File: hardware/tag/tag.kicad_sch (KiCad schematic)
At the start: 12 parts

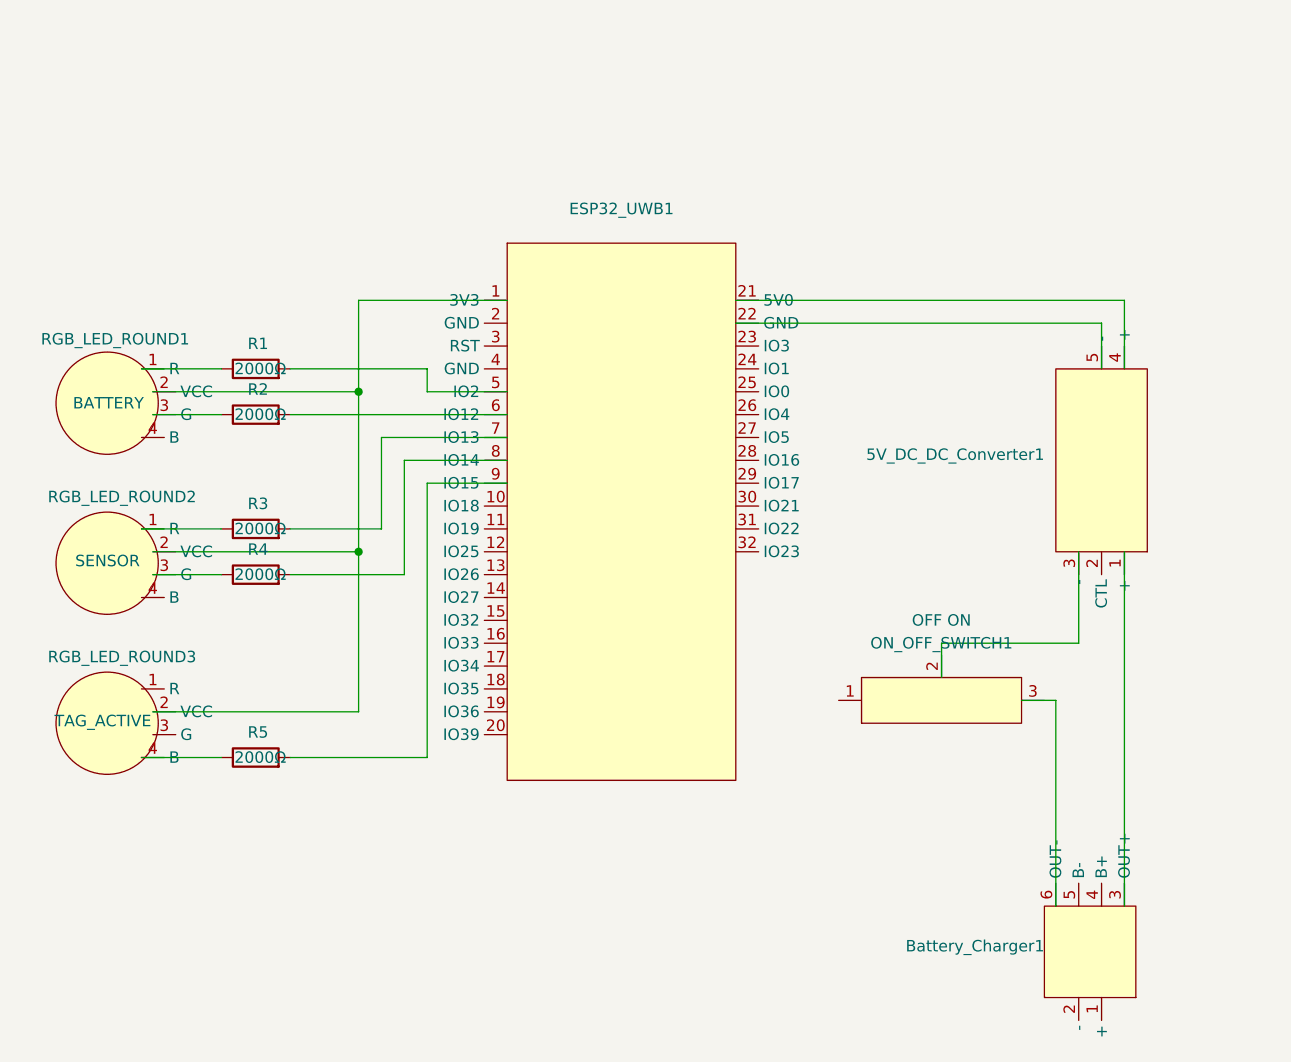
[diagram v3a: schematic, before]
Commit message: remote: Add battery status LED logic.
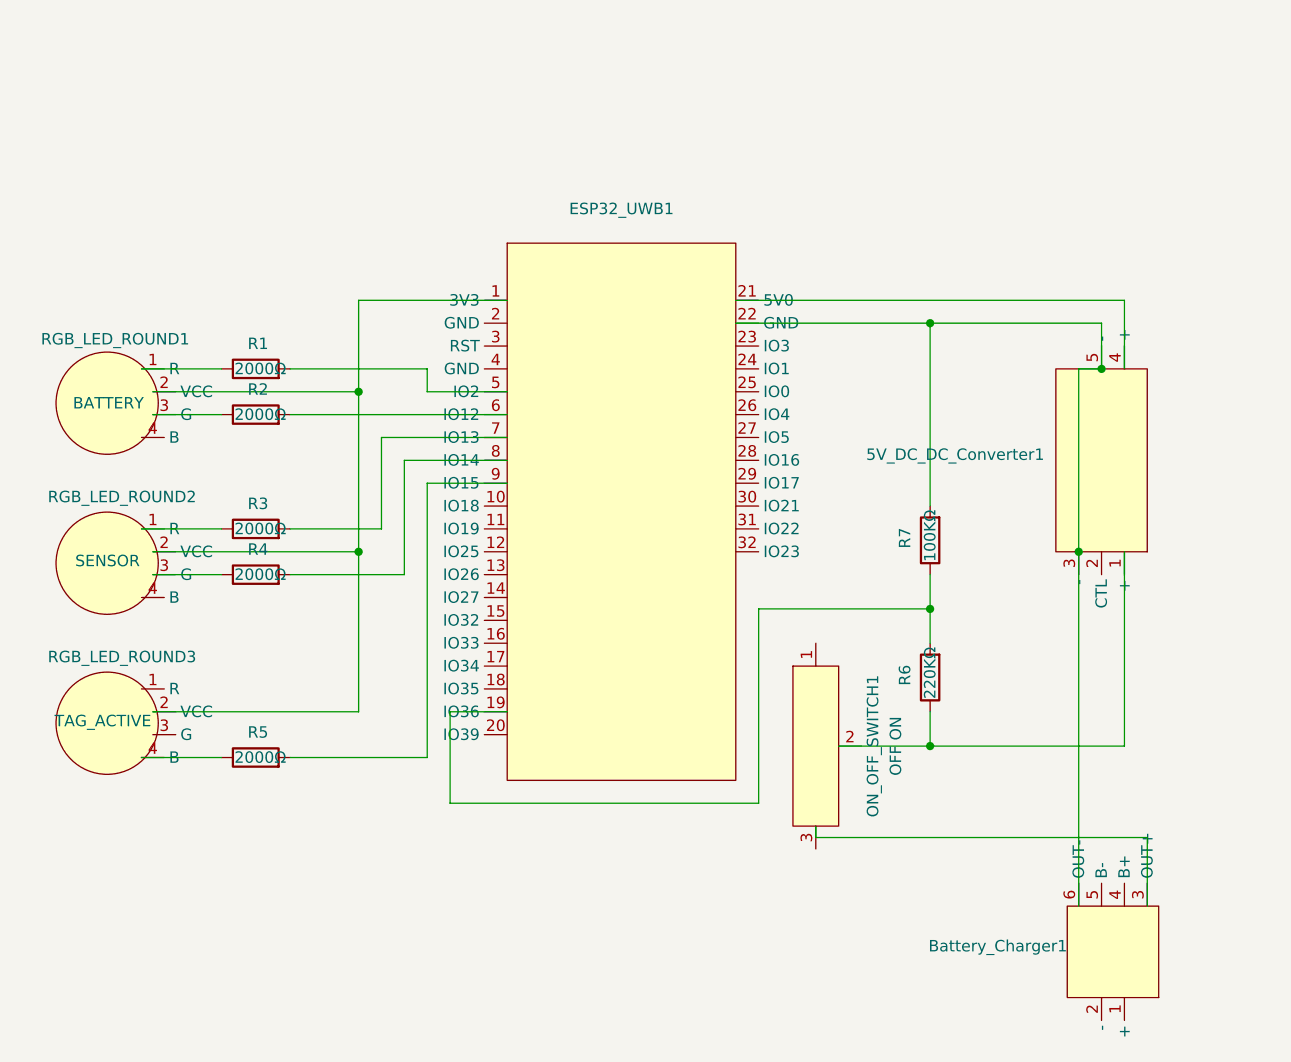
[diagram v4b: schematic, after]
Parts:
- added R6: 220KΩ, Autocam:Simple Resistor, symbol Autocam:Simple Resistor
- added R7: 100KΩ, Autocam:Simple Resistor, symbol Autocam:Simple Resistor
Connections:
- net at ESP32_UWB1.19 (IO36): now also R6.2, R7.1
- net at 5V_DC_DC_Converter1.5 (-), ESP32_UWB1.22 (GND): now also 5V_DC_DC_Converter1.3 (-), Battery_Charger1.6 (OUT-), R7.2
- net at 5V_DC_DC_Converter1.1 (+): now also ON_OFF_SWITCH1.2, R6.1; no longer Battery_Charger1.3 (OUT+)
- net at ON_OFF_SWITCH1.3: now also Battery_Charger1.3 (OUT+); no longer Battery_Charger1.6 (OUT-)
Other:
- moved on the sheet: Battery_Charger1, ON_OFF_SWITCH1

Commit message: hardware/tag: Remove the tag active led.
The tag has not turned on the BLE yet.
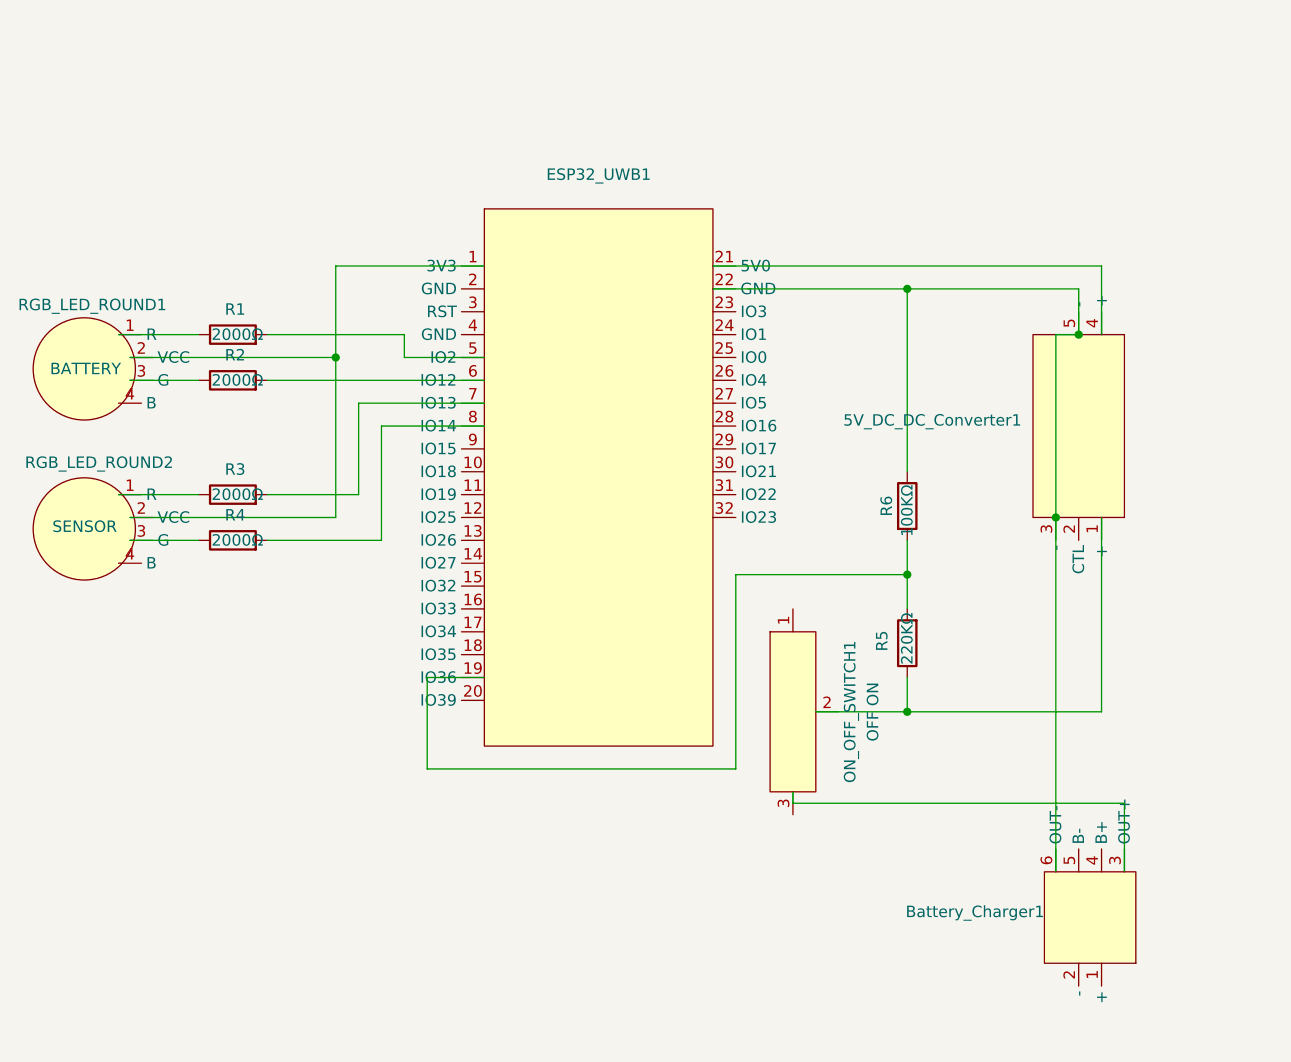
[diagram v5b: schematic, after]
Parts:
- removed R5: 2000Ω, Autocam:Simple Resistor, symbol Autocam:Simple Resistor
- removed RGB_LED_ROUND3: TAG_ACTIVE, Autocam:Anode RGB LED (Round), symbol Autocam:ANODE_RGB_LED_Round
- renumbered R6 to R5, R7 to R6
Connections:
- net at ESP32_UWB1.19 (IO36), R5.2: now also R6.2; no longer R6.1
- net at 5V_DC_DC_Converter1.3 (-), 5V_DC_DC_Converter1.5 (-), Battery_Charger1.6 (OUT-)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: now also R6.1; no longer R6.2
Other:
- moved on the sheet: 5V_DC_DC_Converter1, Battery_Charger1, ESP32_UWB1, ON_OFF_SWITCH1, R1, R2, R3, R4, R5, R6, RGB_LED_ROUND1, RGB_LED_ROUND2

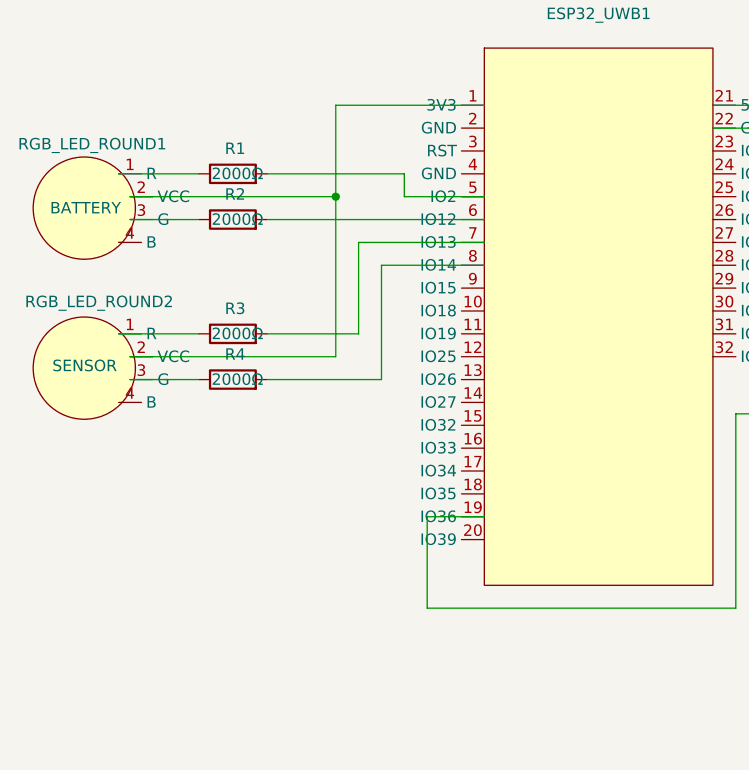
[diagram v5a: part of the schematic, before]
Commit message: hardware: Increase the LED resistor from 2000Ω to 10KΩ.
To reduce the power consumption.
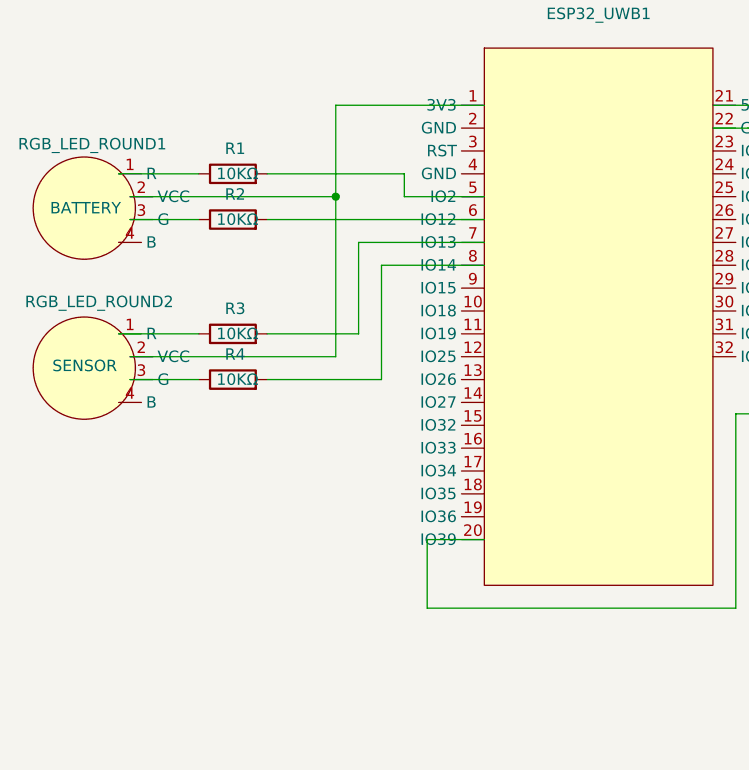
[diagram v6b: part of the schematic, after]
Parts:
- R1, R2, R3, R4: value 2000Ω -> 10KΩ
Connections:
- net at R5.2, R6.2: now also ESP32_UWB1.20 (IO39); no longer ESP32_UWB1.19 (IO36)
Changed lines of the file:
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@@
+	(wire
+		(pts
+			(xy 127 132.08) (xy 127 124.46)
+		)
+		(stroke
+			(width 0)
+			(type default)
+		)
+	)
 	(wire
 		(pts
@@
 	(wire
 		(pts
+			(xy 127 124.46) (xy 133.35 124.46)
+		)
+		(stroke
+			(width 0)
+			(type default)
+		)
+	)
+	(wire
+		(pts
 			(xy 116.84 76.2) (xy 133.35 76.2)
 		)
@@
 	(wire
 		(pts
-			(xy 133.35 121.92) (xy 127 121.92)
-		)
-		(stroke
-			(width 0)
-			(type default)
-		)
-	)
-	(wire
-		(pts
 			(xy 201.93 83.82) (xy 201.93 76.2)
 		)
@@
 		(pts
 			(xy 109.22 106.68) (xy 121.92 106.68)
-		)
-		(stroke
-			(width 0)
-			(type default)
-		)
-	)
-	(wire
-		(pts
-			(xy 127 121.92) (xy 127 132.08)
 		)
 		(stroke
@@
 			)
 		)
-		(property "Value" "2000Ω"
+		(property "Value" "10KΩ"
 			(at 105.918 106.68 90)
 			(effects
@@
 			)
 		)
-		(property "Value" "2000Ω"
+		(property "Value" "10KΩ"
 			(at 105.918 101.6 90)
 			(effects
@@
 			)
 		)
-		(property "Value" "2000Ω"
+		(property "Value" "10KΩ"
 			(at 105.918 83.82 90)
 			(effects
@@
 			)
 		)
-		(property "Value" "2000Ω"
+		(property "Value" "10KΩ"
 			(at 105.918 88.9 90)
 			(effects

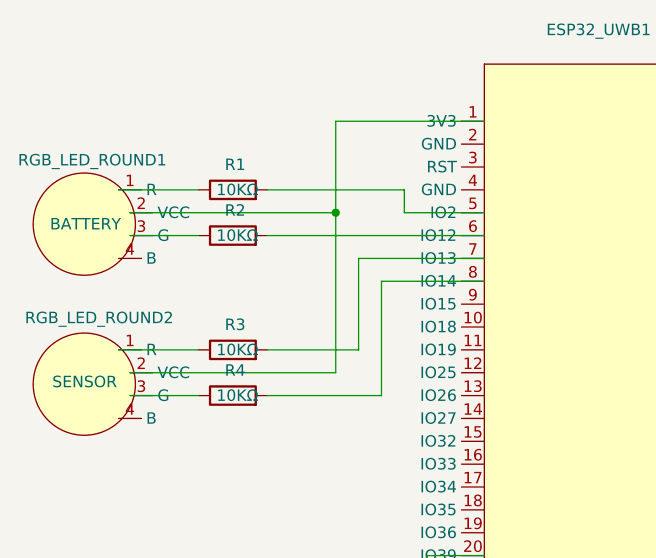
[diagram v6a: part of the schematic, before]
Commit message: hardware: Reroute the wires to fix unavailable PINs.
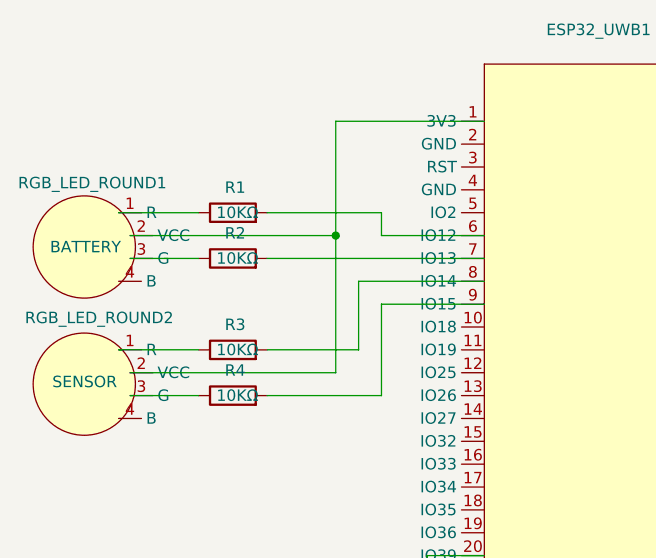
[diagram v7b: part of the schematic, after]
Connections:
- net at R4.2: now also ESP32_UWB1.9 (IO15); no longer ESP32_UWB1.8 (IO14)
- net at R3.2: now also ESP32_UWB1.8 (IO14); no longer ESP32_UWB1.7 (IO13)
- net at ESP32_UWB1.5 (IO2): no longer R1.2
- net at ESP32_UWB1.6 (IO12): now also R1.2; no longer R2.2
- new net: ESP32_UWB1.7 (IO13), R2.2
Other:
- moved on the sheet: R1, R2, RGB_LED_ROUND1
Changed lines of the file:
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@@
 	)
 	(junction
-		(at 116.84 86.36)
+		(at 116.84 88.9)
 		(diameter 0)
 		(color 0 0 0 0)
@@
 	(wire
 		(pts
+			(xy 116.84 76.2) (xy 116.84 88.9)
+		)
+		(stroke
+			(width 0)
+			(type default)
+		)
+	)
+	(wire
+		(pts
 			(xy 180.34 78.74) (xy 180.34 99.06)
 		)
@@
 	(wire
 		(pts
-			(xy 124.46 86.36) (xy 133.35 86.36)
-		)
-		(stroke
-			(width 0)
-			(type default)
-		)
-	)
-	(wire
-		(pts
-			(xy 116.84 76.2) (xy 116.84 86.36)
-		)
-		(stroke
-			(width 0)
-			(type default)
-		)
-	)
-	(wire
-		(pts
 			(xy 204.47 143.51) (xy 204.47 135.89)
 		)
@@
 	(wire
 		(pts
-			(xy 93.98 88.9) (xy 101.6 88.9)
+			(xy 93.98 91.44) (xy 101.6 91.44)
 		)
 		(stroke
@@
 	(wire
 		(pts
-			(xy 109.22 88.9) (xy 133.35 88.9)
+			(xy 133.35 88.9) (xy 121.92 88.9)
+		)
+		(stroke
+			(width 0)
+			(type default)
+		)
+	)
+	(wire
+		(pts
+			(xy 119.38 93.98) (xy 133.35 93.98)
 		)
 		(stroke
@@
 	(wire
 		(pts
-			(xy 124.46 83.82) (xy 124.46 86.36)
-		)
-		(stroke
-			(width 0)
-			(type default)
-		)
-	)
-	(wire
-		(pts
-			(xy 119.38 101.6) (xy 119.38 91.44)
-		)
-		(stroke
-			(width 0)
-			(type default)
-		)
-	)
-	(wire
-		(pts
-			(xy 119.38 91.44) (xy 133.35 91.44)
+			(xy 119.38 101.6) (xy 119.38 93.98)
 		)
 		(stroke
@@
 	(wire
 		(pts
-			(xy 93.98 86.36) (xy 116.84 86.36)
+			(xy 93.98 88.9) (xy 116.84 88.9)
 		)
 		(stroke
@@
 	(wire
 		(pts
+			(xy 121.92 88.9) (xy 121.92 86.36)
+		)
+		(stroke
+			(width 0)
+			(type default)
+		)
+	)
+	(wire
+		(pts
+			(xy 116.84 88.9) (xy 116.84 104.14)
+		)
+		(stroke
+			(width 0)
+			(type default)
+		)
+	)
+	(wire
+		(pts
 			(xy 116.84 76.2) (xy 133.35 76.2)
 		)
@@
 	(wire
 		(pts
-			(xy 121.92 93.98) (xy 133.35 93.98)
-		)
-		(stroke
-			(width 0)
-			(type default)
-		)
-	)
-	(wire
-		(pts
-			(xy 121.92 106.68) (xy 121.92 93.98)
+			(xy 121.92 106.68) (xy 121.92 96.52)
 		)
 		(stroke
@@
 	(wire
 		(pts
-			(xy 109.22 83.82) (xy 124.46 83.82)
-		)
-		(stroke
-			(width 0)
-			(type default)
-		)
-	)
-	(wire
-		(pts
-			(xy 116.84 86.36) (xy 116.84 104.14)
+			(xy 109.22 86.36) (xy 121.92 86.36)
 		)
 		(stroke
@@
 	(wire
 		(pts
+			(xy 133.35 91.44) (xy 109.22 91.44)
+		)
+		(stroke
+			(width 0)
+			(type default)
+		)
+	)
+	(wire
+		(pts
 			(xy 180.34 78.74) (xy 199.39 78.74)
 		)
@@
 	(wire
 		(pts
-			(xy 92.71 83.82) (xy 101.6 83.82)
+			(xy 92.71 86.36) (xy 101.6 86.36)
 		)
 		(stroke
@@
 		(pts
 			(xy 201.93 83.82) (xy 201.93 76.2)
+		)
+		(stroke
+			(width 0)
+			(type default)
+		)
+	)
+	(wire
+		(pts
+			(xy 121.92 96.52) (xy 133.35 96.52)
 		)
 		(stroke
@@
 	(symbol
 		(lib_id "Autocam:ANODE_RGB_LED_Round")
-		(at 88.9 87.63 0)
+		(at 88.9 90.17 0)
 		(mirror y)
 		(unit 1)
@@
 		(dnp no)
 		(property "Reference" "RGB_LED_ROUND1"
-			(at 81.534 80.518 0)
+			(at 81.534 83.058 0)
 			(effects
 				(font
@@
 		)
 		(property "Value" "BATTERY"
-			(at 85.09 87.63 0)
+			(at 85.09 90.17 0)
 			(effects
 				(font
@@
 		)
 		(property "Footprint" "Autocam:Anode RGB LED (Round)"
-			(at 93.98 83.82 0)
+			(at 93.98 86.36 0)
 			(effects
 				(font
@@
 		)
 		(property "Datasheet" ""
-			(at 93.98 83.82 0)
+			(at 93.98 86.36 0)
 			(effects
 				(font
@@
 		)
 		(property "Description" ""
-			(at 93.98 83.82 0)
+			(at 93.98 86.36 0)
 			(effects
 				(font
@@
 	(symbol
 		(lib_id "Autocam:Simple Resistor")
-		(at 105.41 83.82 90)
+		(at 105.41 86.36 90)
 		(unit 1)
 		(exclude_from_sim no)
@@
 		(dnp no)
 		(property "Reference" "R1"
-			(at 105.664 81.026 90)
+			(at 105.664 83.566 90)
 			(effects
 				(font
@@
 		)
 		(property "Value" "10KΩ"
-			(at 105.918 83.82 90)
+			(at 105.918 86.36 90)
 			(effects
 				(font
@@
 		)
 		(property "Footprint" "Autocam:Simple Resistor"
-			(at 105.41 85.598 90)
+			(at 105.41 88.138 90)
 			(effects
 				(font
@@
 		)
 		(property "Datasheet" "~"
-			(at 105.41 83.82 0)
+			(at 105.41 86.36 0)
 			(effects
 				(font
@@
 		)
 		(property "Description" "Resistor"
-			(at 105.41 83.82 0)
+			(at 105.41 86.36 0)
 			(effects
 				(font
@@
 	(symbol
 		(lib_id "Autocam:Simple Resistor")
-		(at 105.41 88.9 90)
+		(at 105.41 91.44 90)
 		(unit 1)
 		(exclude_from_sim no)
@@
 		(dnp no)
 		(property "Reference" "R2"
-			(at 105.664 86.106 90)
+			(at 105.664 88.646 90)
 			(effects
 				(font
@@
 		)
 		(property "Value" "10KΩ"
-			(at 105.918 88.9 90)
+			(at 105.918 91.44 90)
 			(effects
 				(font
@@
 		)
 		(property "Footprint" "Autocam:Simple Resistor"
-			(at 105.41 90.678 90)
+			(at 105.41 93.218 90)
 			(effects
 				(font
@@
 		)
 		(property "Datasheet" "~"
-			(at 105.41 88.9 0)
+			(at 105.41 91.44 0)
 			(effects
 				(font
@@
 		)
 		(property "Description" "Resistor"
-			(at 105.41 88.9 0)
-			(effects
-				(font
+			(at 105.41 91.44 0)
+			(effects
+				(font
